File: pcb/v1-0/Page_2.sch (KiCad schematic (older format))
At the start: 54 parts

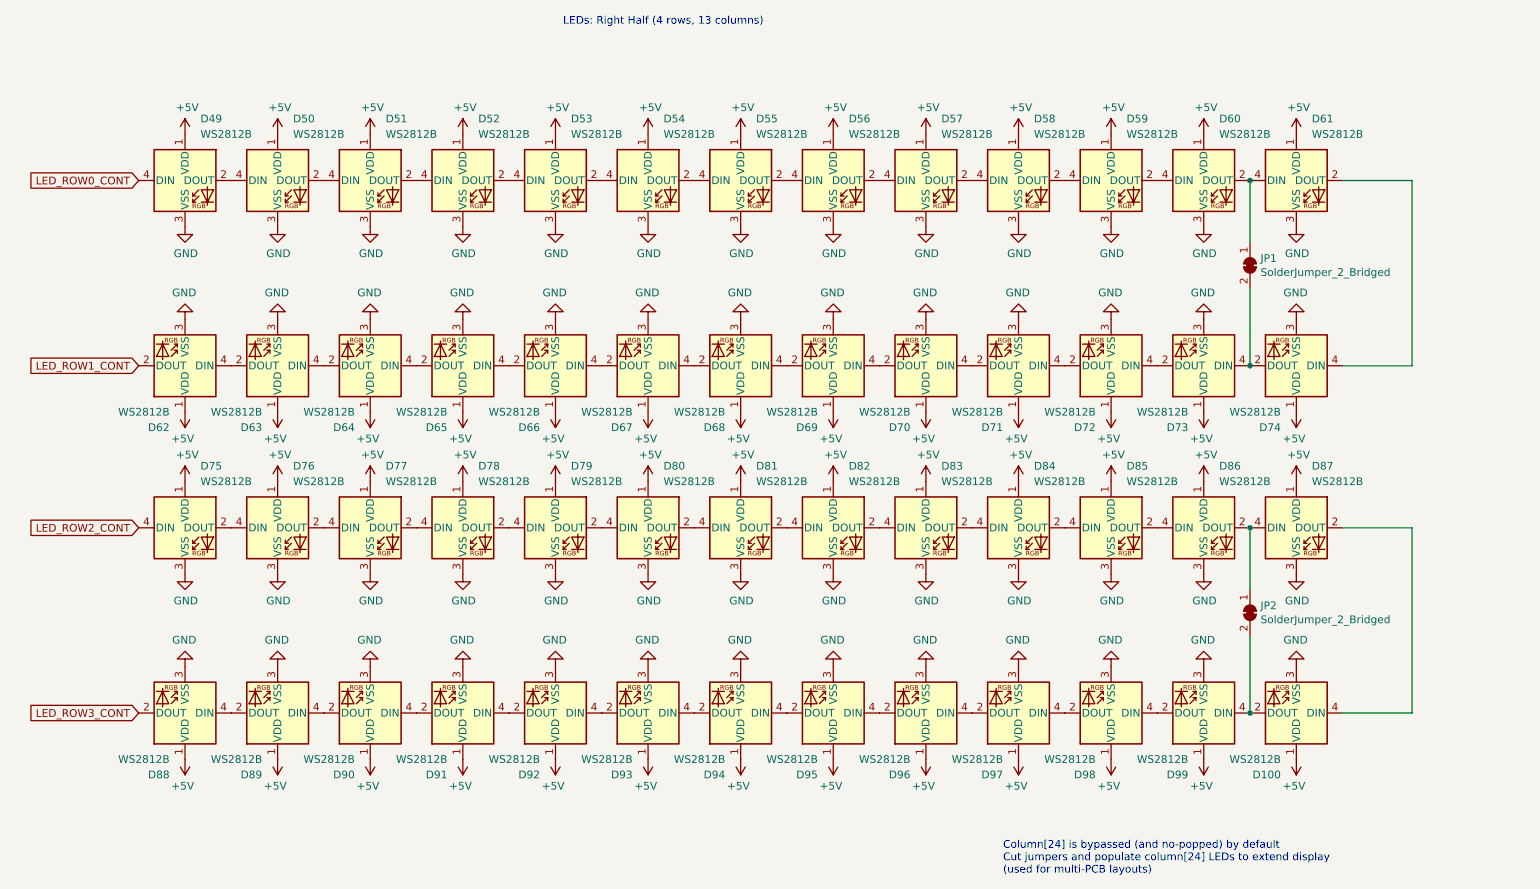
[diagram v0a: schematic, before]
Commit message: link schematic leds to layout
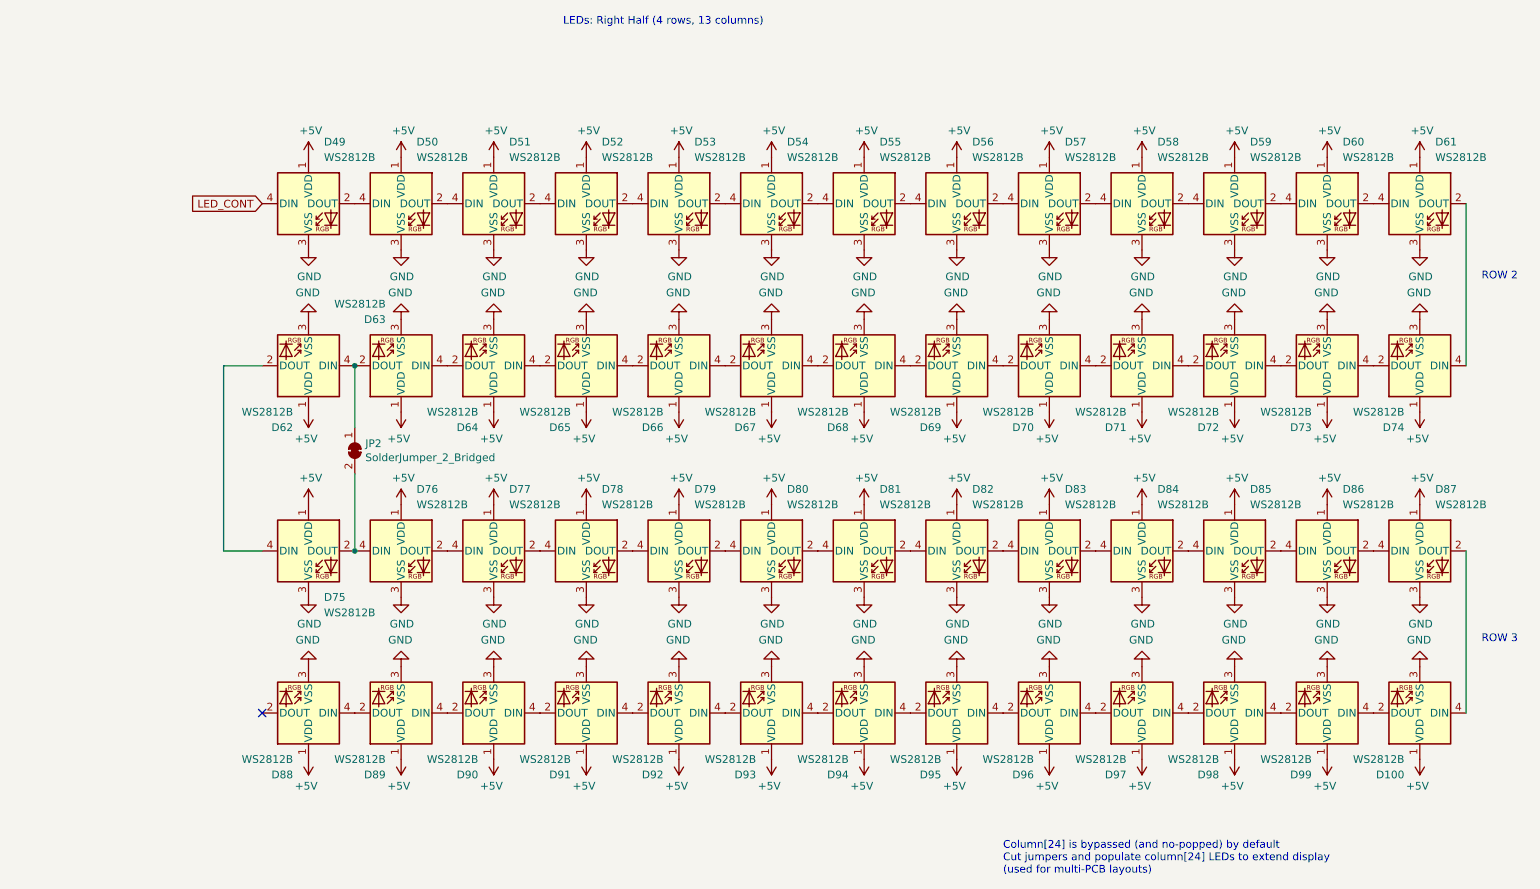
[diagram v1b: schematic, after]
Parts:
- removed JP1: SolderJumper_2_Bridged, Jumper:SolderJumper-2_P1.3mm_Bridged_RoundedPad1.0x1.5mm, symbol Jumper:SolderJumper_2_Bridged
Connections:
- net LED_ROW2_CONT is gone; now on an unnamed net: D75.4 (DIN)
- net at D86.2 (DOUT), D87.4 (DIN): no longer JP2.1 (A)
- net at D100.2 (DOUT), D99.4 (DIN): no longer JP2.2 (B)
- net at D62.4 (DIN), D63.2 (DOUT): now also JP2.1 (A)
- net at D75.2 (DOUT), D76.4 (DIN): now also JP2.2 (B)
- net LED_ROW0_CONT renamed LED_CONT
- net LED_ROW1_CONT: no longer names the net of D62.2 (DOUT)
- net LED_ROW3_CONT: no longer names the net of D88.2 (DOUT)
- no-connect marks 0 -> 1
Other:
- note added: "ROW 2"
- note added: "ROW 3"
- moved on the sheet: D100, D49, D50, D51, D52, D53, D54, D55, D56, D57, D58, D59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

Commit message: consider program over custom USB and remove 100 mil UPDI header
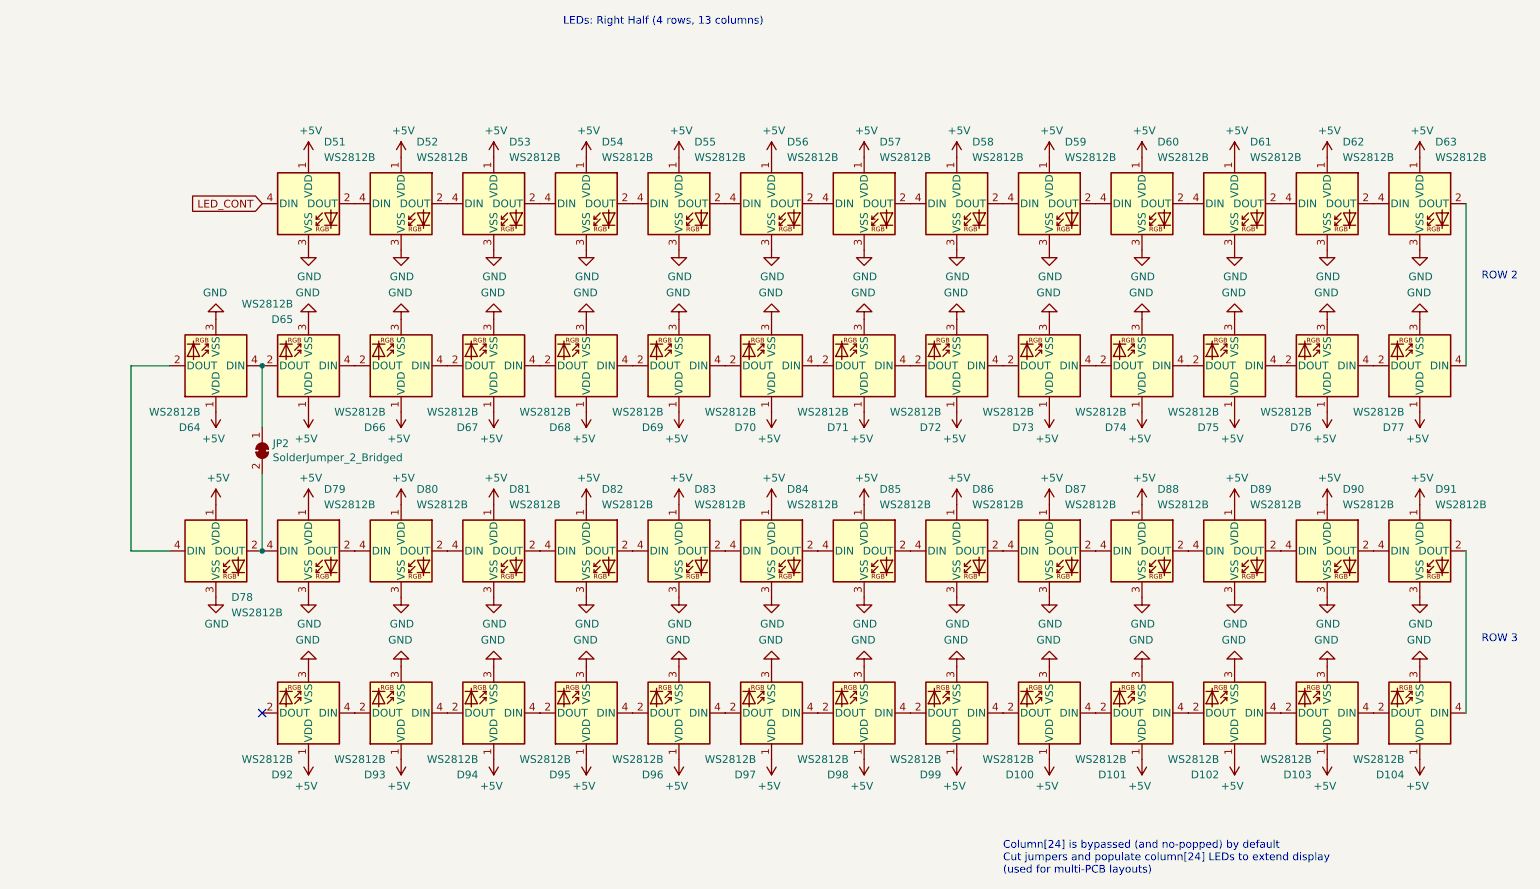
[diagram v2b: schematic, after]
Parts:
- added D66, D80: WS2812B, WS2812B:LED_WS2812B_PLCC4_5.0x5.0mm_P3.2mm, symbol LED:WS2812B
- renumbered D96 to D100, D97 to D101, D98 to D102, D99 to D103, D100 to D104, D49 to D51, D50 to D52, D51 to D53, D52 to D54, D53 to D55, D54 to D56, D55 to D57, D56 to D58, D57 to D59, D58 to D60, D59 to D61, D60 to D62, D61 to D63, D62 to D64, D63 to D65, D64 to D67, D65 to D68, D66 to D69, D67 to D70, D68 to D71, D69 to D72, D70 to D73, D71 to D74, D72 to D75, D73 to D76, D74 to D77, D75 to D78, D76 to D79, D77 to D81, D78 to D82, D79 to D83, D80 to D84, D81 to D85, D82 to D86, D83 to D87, D84 to D88, D85 to D89, D86 to D90, D87 to D91, D88 to D92, D89 to D93, D90 to D94, D91 to D95, D92 to D96, D93 to D97, D94 to D98, D95 to D99
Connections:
- net +5V: now also D66.1 (VDD), D80.1 (VDD)
- net GND: now also D66.3 (VSS), D80.3 (VSS)
- net at D65.4 (DIN): now also D66.2 (DOUT); no longer D67.2 (DOUT)
- net at D79.2 (DOUT): now also D80.4 (DIN); no longer D81.4 (DIN)
- new net: D80.2 (DOUT), D81.4 (DIN)
- new net: D66.4 (DIN), D67.2 (DOUT)
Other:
- moved on the sheet: D64, D65, D78, D79, JP2

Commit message: compontnets placedr
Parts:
- removed D104, D63, D77, D91: WS2812B, WS2812B:LED_WS2812B_PLCC4_5.0x5.0mm_P3.2mm, symbol LED:WS2812B
- renumbered D103 to D100, D64 to D63, D65 to D64, D66 to D65, D67 to D66, D68 to D67, D69 to D68, D70 to D69, D71 to D70, D72 to D71, D73 to D72, D74 to D73, D75 to D74, D76 to D75, D78 to D76, D79 to D77, D80 to D78, D81 to D79, D82 to D80, D83 to D81, D84 to D82, D85 to D83, D86 to D84, D87 to D85, D88 to D86, D89 to D87, D90 to D88, D92 to D89, D93 to D90, D94 to D91, D95 to D92, D96 to D93, D97 to D94, D98 to D95, D99 to D96, D100 to D97, D101 to D98, D102 to D99
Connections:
- net +5V: no longer D60.1 (VDD)
- net at D62.2 (DOUT): now also D75.4 (DIN)
- net at D100.4 (DIN): now also D88.2 (DOUT)

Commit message: candidate draft
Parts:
- added C4, C5: 2u2, Capacitor_SMD:C_0805_2012Metric, symbol Device:C
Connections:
- net +5V: now also C4.2, C5.2
- net GND: now also C4.1, C5.1
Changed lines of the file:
@@
 	-1   0    0    1
 $EndComp
+$Comp
+L Device:C C?
+U 1 1 5F8061A5
+P 1550 1800
+AR Path="/5F0AD215/5F8061A5" Ref="C?"  Part="1"
+AR Path="/5F1120A6/5F8061A5" Ref="C4"  Part="1"
+F 0 "C4" V 1298 1800 50  0000 C CNN
+F 1 "2u2" V 1389 1800 50  0000 C CNN
+F 2 "Capacitor_SMD:C_0805_2012Metric" H 1588 1650 50  0001 C CNN
+F 3 "~" H 1550 1800 50  0001 C CNN
+	1    1550 1800
+	-1   0    0    1
+$EndComp
+$Comp
+L power:+5V #PWR?
+U 1 1 5F8061AB
+P 1550 1650
+AR Path="/5F0AD215/5F8061AB" Ref="#PWR?"  Part="1"
+AR Path="/5F1120A6/5F8061AB" Ref="#PWR0222"  Part="1"
+F 0 "#PWR0222" H 1550 1500 50  0001 C CNN
+F 1 "+5V" H 1565 1823 50  0000 C CNN
+F 2 "" H 1550 1650 50  0001 C CNN
+F 3 "" H 1550 1650 50  0001 C CNN
+	1    1550 1650
+	1    0    0    -1
+$EndComp
+$Comp
+L power:GND #PWR?
+U 1 1 5F8061B1
+P 1550 1950
+AR Path="/5F0AD215/5F8061B1" Ref="#PWR?"  Part="1"
+AR Path="/5F1120A6/5F8061B1" Ref="#PWR0223"  Part="1"
+F 0 "#PWR0223" H 1550 1700 50  0001 C CNN
+F 1 "GND" H 1555 1777 50  0000 C CNN
+F 2 "" H 1550 1950 50  0001 C CNN
+F 3 "" H 1550 1950 50  0001 C CNN
+	1    1550 1950
+	1    0    0    -1
+$EndComp
+$Comp
+L Device:C C?
+U 1 1 5F806BB7
+P 1500 5450
+AR Path="/5F0AD215/5F806BB7" Ref="C?"  Part="1"
+AR Path="/5F1120A6/5F806BB7" Ref="C5"  Part="1"
+F 0 "C5" V 1248 5450 50  0000 C CNN
+F 1 "2u2" V 1339 5450 50  0000 C CNN
+F 2 "Capacitor_SMD:C_0805_2012Metric" H 1538 5300 50  0001 C CNN
+F 3 "~" H 1500 5450 50  0001 C CNN
+	1    1500 5450
+	-1   0    0    1
+$EndComp
+$Comp
+L power:+5V #PWR?
+U 1 1 5F806BBD
+P 1500 5300
+AR Path="/5F0AD215/5F806BBD" Ref="#PWR?"  Part="1"
+AR Path="/5F1120A6/5F806BBD" Ref="#PWR0224"  Part="1"
+F 0 "#PWR0224" H 1500 5150 50  0001 C CNN
+F 1 "+5V" H 1515 5473 50  0000 C CNN
+F 2 "" H 1500 5300 50  0001 C CNN
+F 3 "" H 1500 5300 50  0001 C CNN
+	1    1500 5300
+	1    0    0    -1
+$EndComp
+$Comp
+L power:GND #PWR?
+U 1 1 5F806BC3
+P 1500 5600
+AR Path="/5F0AD215/5F806BC3" Ref="#PWR?"  Part="1"
+AR Path="/5F1120A6/5F806BC3" Ref="#PWR0225"  Part="1"
+F 0 "#PWR0225" H 1500 5350 50  0001 C CNN
+F 1 "GND" H 1505 5427 50  0000 C CNN
+F 2 "" H 1500 5600 50  0001 C CNN
+F 3 "" H 1500 5600 50  0001 C CNN
+	1    1500 5600
+	1    0    0    -1
+$EndComp
 $EndSCHEMATC
